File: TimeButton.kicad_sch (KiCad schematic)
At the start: 27 parts, among them J1 USB_C_Receptacle_USB2.0_16P, J2 TagConnect, J3 Conn_01x05_Pin, J4 Conn_01x03_Pin, SW1 SW_Push, U1 PIC18F15Q41-I/SS, U2 FT231XS

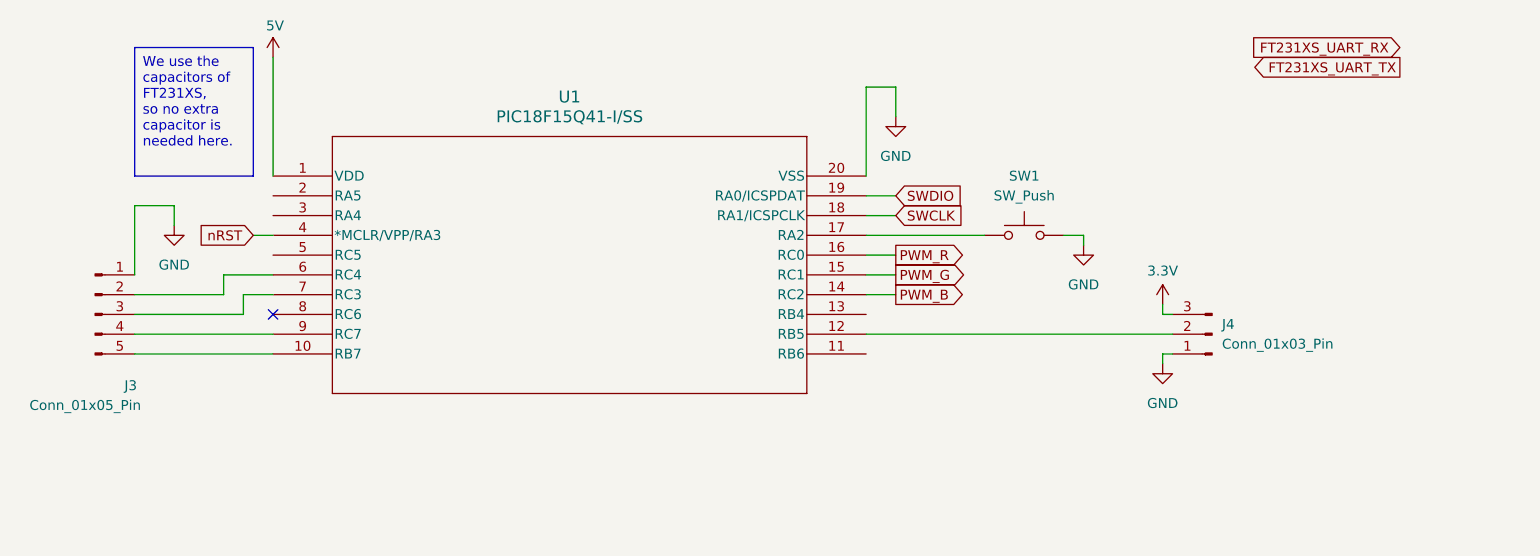
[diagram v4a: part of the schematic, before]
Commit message: Added UART connection to FT231XS + changed some pin outputs as a result to fit it into the design
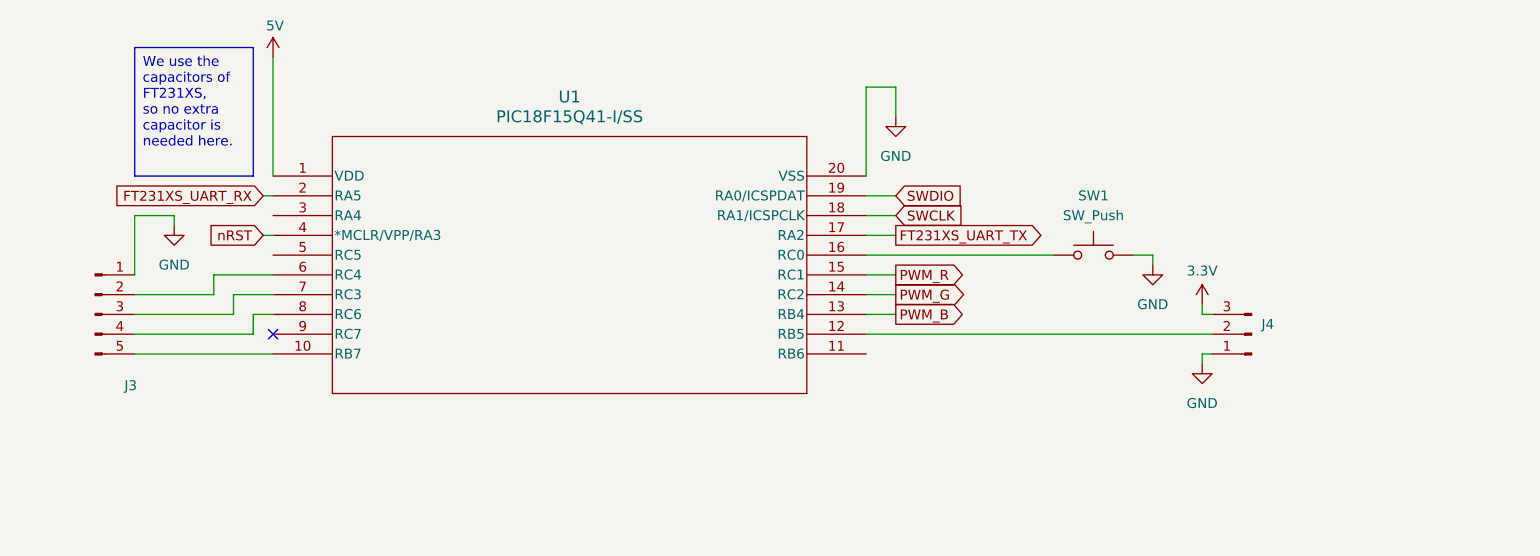
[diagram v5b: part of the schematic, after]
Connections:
- net FT231XS_UART_RX: now also U1.2 (RA5)
- net FT231XS_UART_TX: now also U1.17 (RA2)
- net PWM_B: now also U1.13 (RB4); no longer U1.14 (RC2)
- net PWM_G: now also U1.14 (RC2); no longer U1.15 (RC1)
- net PWM_R: now also U1.15 (RC1); no longer U1.16 (RC0)
- net at J3.4 (Pin_4): now also U1.8 (RC6); no longer U1.9 (RC7)
- net at SW1.2: now also U1.16 (RC0); no longer U1.17 (RA2)
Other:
- moved on the sheet: J4

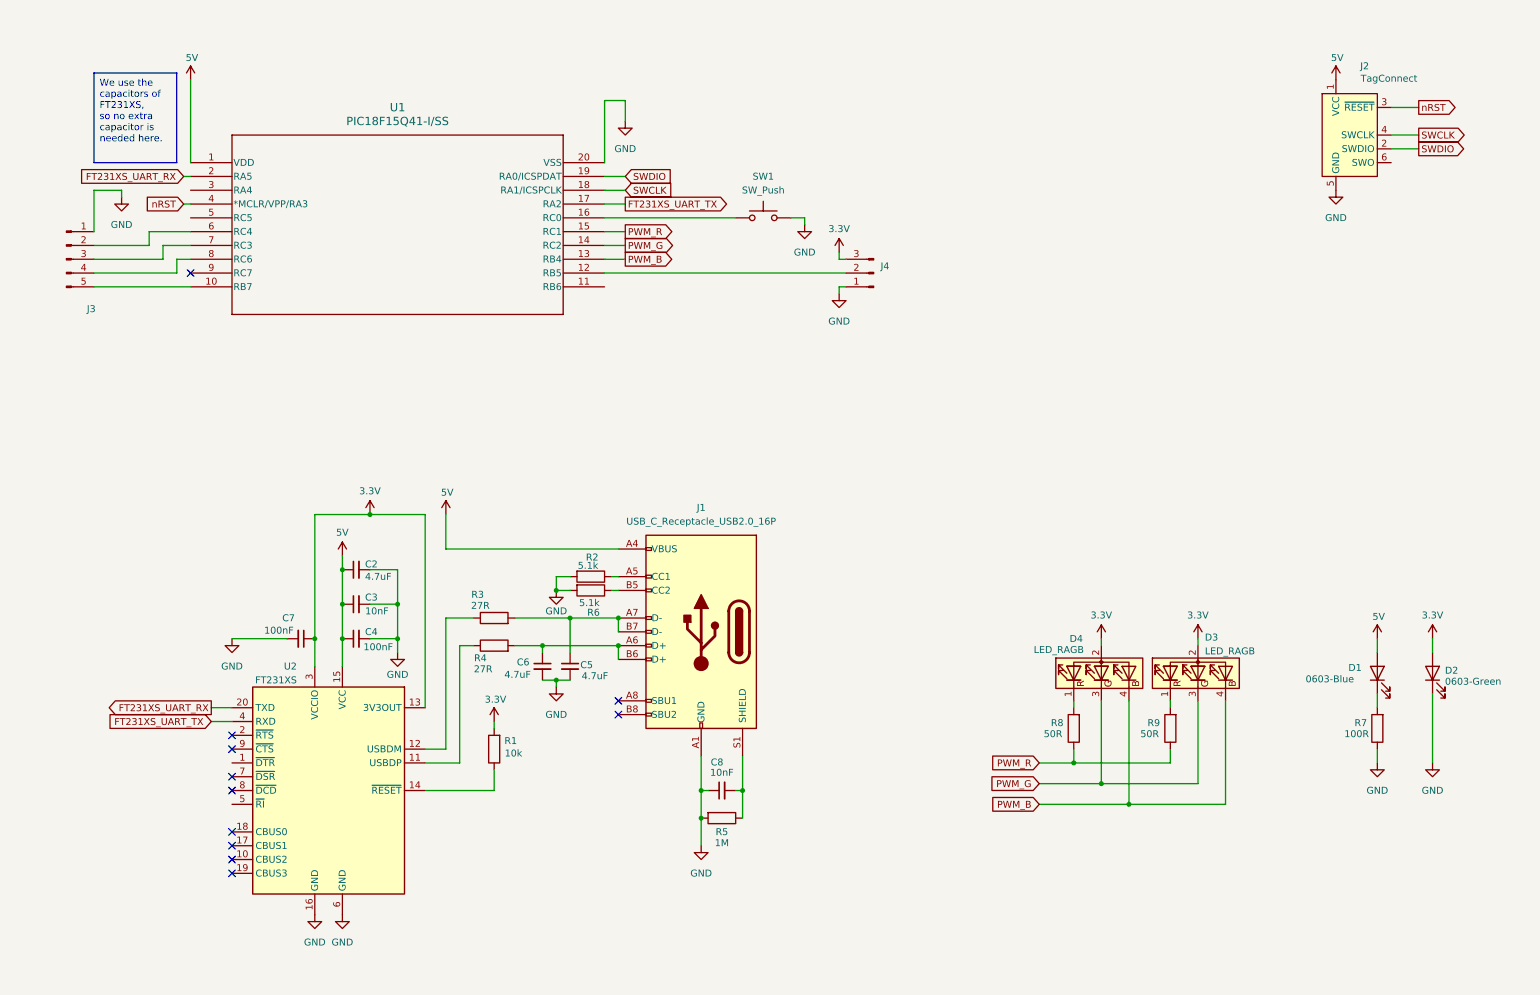
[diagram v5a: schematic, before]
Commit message: Updated layout
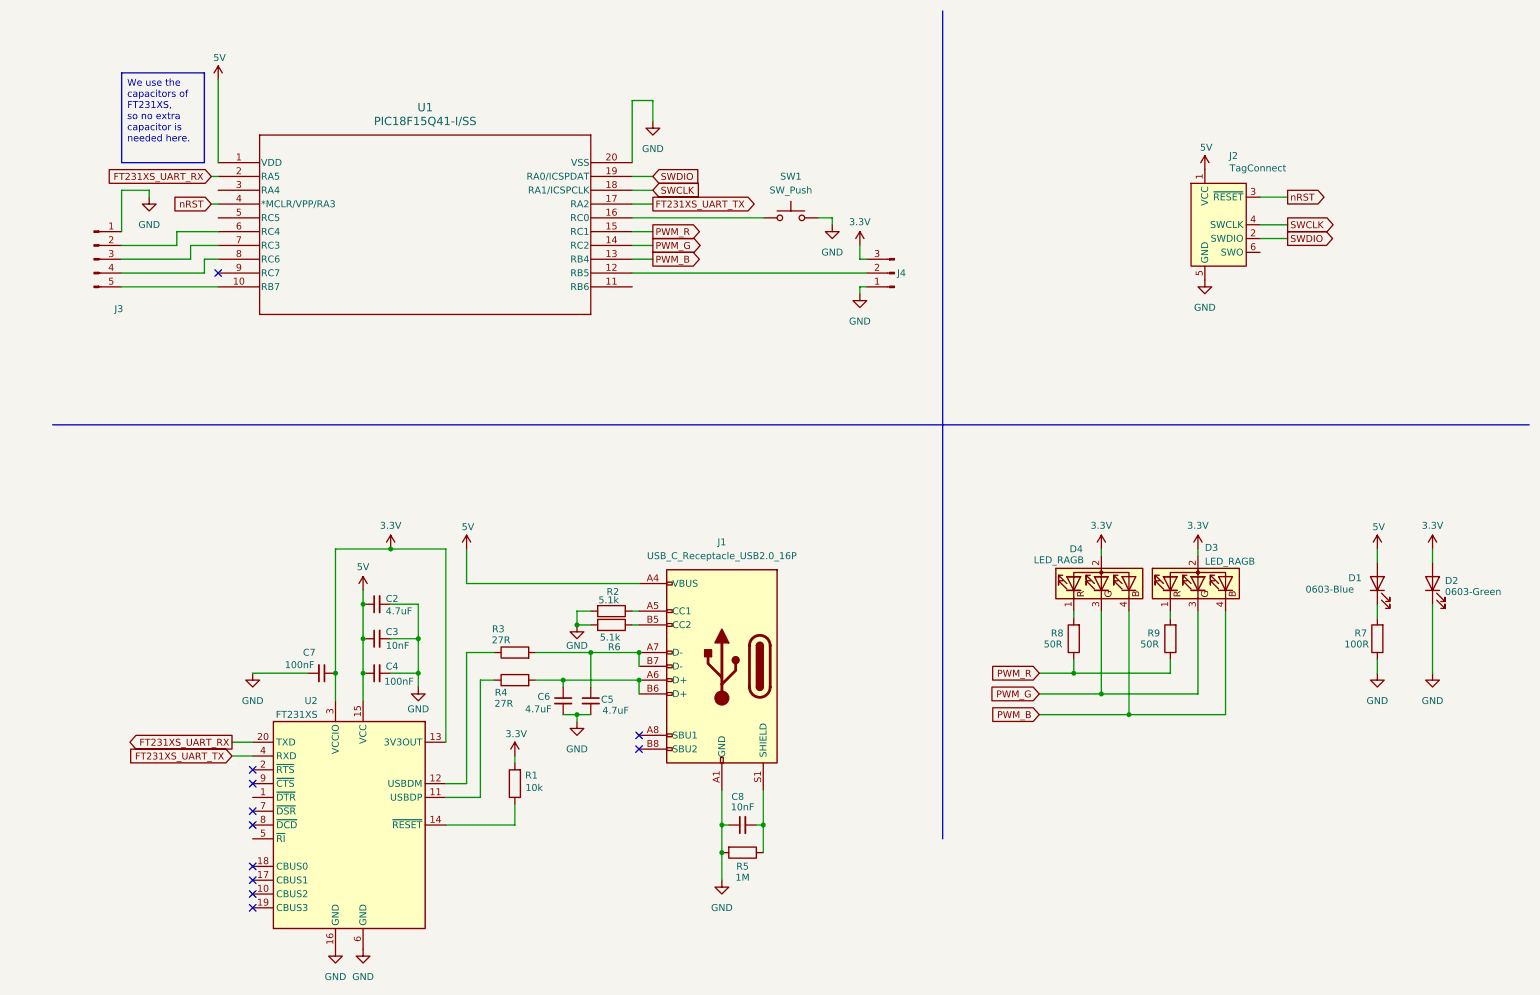
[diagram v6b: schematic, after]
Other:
- title: (none) -> TimeButton
- moved on the sheet: C2, C3, C4, C5, C6, C7, C8, D1, D2, D3, D4, J1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
